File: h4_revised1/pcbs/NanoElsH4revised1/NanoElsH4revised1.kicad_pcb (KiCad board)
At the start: 4 copper layers, 141 x 86 mm, 142 parts, among them Q1 SI2302ADS-T1, Q10 SI2302ADS-T1, Q11 SI2302ADS-T1, Q12 SI2302ADS-T1, Q13 SI2302ADS-T1, Q14 SI2302ADS-T1, Q15 SI2302ADS-T1, Q16 SI2302ADS-T1, Q18 SI2302ADS-T1, Q2 SI2302ADS-T1, Q3 S9013W, Q4 S9013W, Q5 SI2302ADS-T1, Q6 SI2302ADS-T1, Q7 SI2302ADS-T1, Q8 SI2302ADS-T1, Q9 SI2302ADS-T1

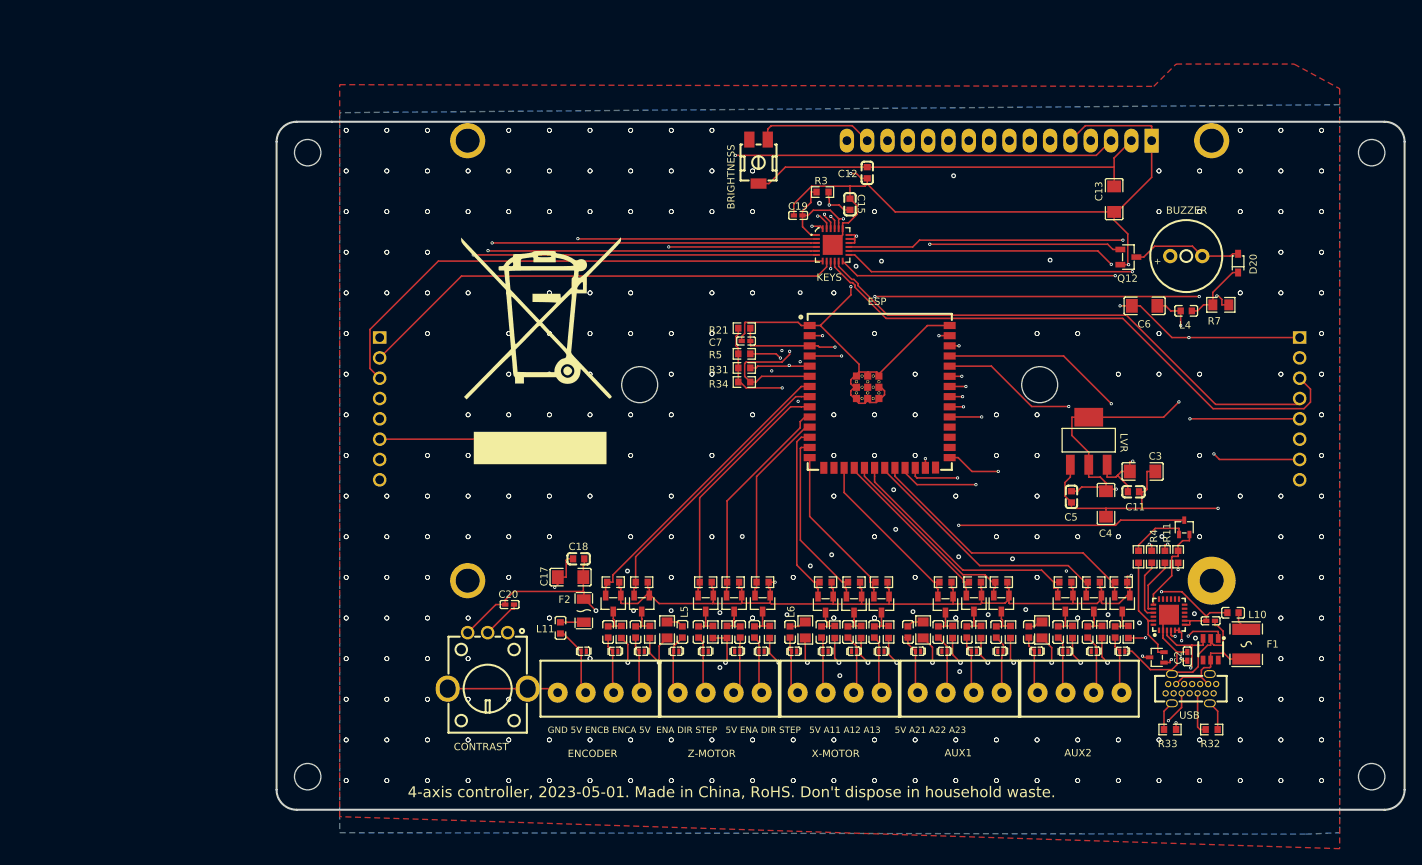
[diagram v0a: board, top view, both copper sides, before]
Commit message: - Added actual KiCad 8 files (layout ready, but some cosmetic documentation ToDo's)
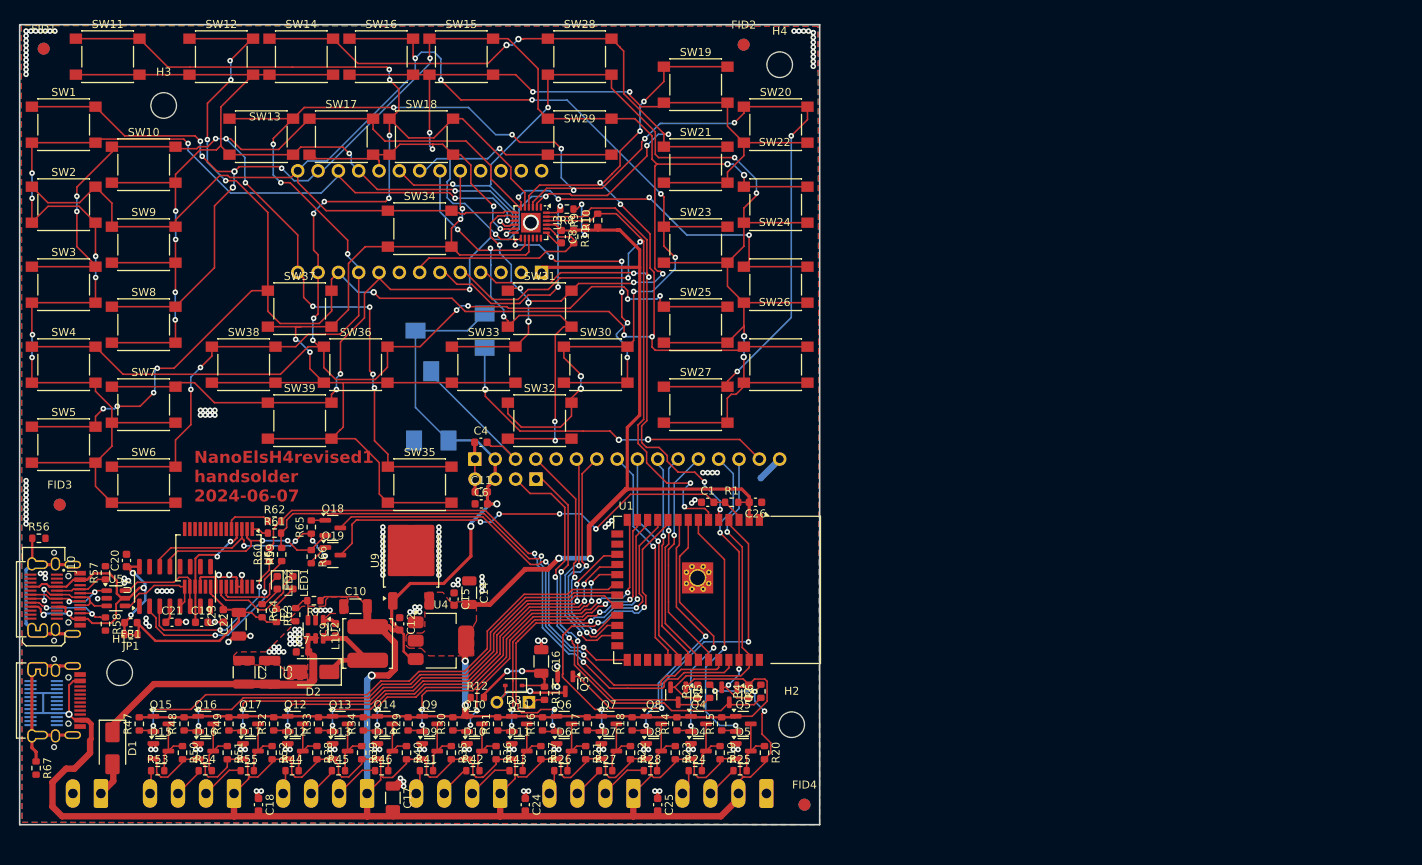
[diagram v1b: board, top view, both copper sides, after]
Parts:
- removed AUX1, AUX2, ENCODER, X-MOTOR, Z-MOTOR: DB2EVC-3.5-4P-GN, NanoElsH4:CONN-TH_4P-P3.50_DB2EVC-3.5-4P-GN
- removed BRIGHTNESS: 1k, NanoElsH4:RES-ADJ-SMD_3P-L4.5-W4.5-P2.30-LS6.2-BL-FS
- removed BUZZER: QMB-09B-03, NanoElsH4:BUZ-TH_BD9.0-P4.00-D0.6-FD
- removed C13, C3: 10uF, NanoElsH4:C1206
- removed COLS, ROWS: MF254V-11-08-0540, NanoElsH4:HDR-TH_8P-P2.54-V-F-3
- removed CONTRAST: 10kΩ, NanoElsH4:RES-TH_RK09K113004U
- removed D20: 1N4148WS T4, NanoElsH4:SOD-323_L1.8-W1.3-LS2.5-RD
- removed D21, D22, D23, D24, D25, D26, D27, D28, D29, D30, D31, D32, D33, D34, D35, D36, D37, D38, D39: KESD9B5VL, NanoElsH4:X1-DFN1006-2_L1.0-W0.6-P0.65-BI
- removed ESP: ESP32-S3-WROOM-1U-N16R2, NanoElsH4:WIRELM-SMD_ESP32-S3-WROOM-1U
- removed F1: SMD1812P030TF, NanoElsH4:F1812
- removed F2: nSMD010, NanoElsH4:F1206
- removed Hole_gge6227889318616504: Hole_gge6227889318616504, NanoElsH4:Hole_gge6227889318616504
- removed Hole_gge6227889318616534: Hole_gge6227889318616534, NanoElsH4:Hole_gge6227889318616534
- removed Hole_gge6227889318616549: Hole_gge6227889318616549, NanoElsH4:Hole_gge6227889318616549
- removed Hole_gge6227889318616564: Hole_gge6227889318616564, NanoElsH4:Hole_gge6227889318616564
- removed Hole_gge813785: Hole_gge813785, NanoElsH4:Hole_gge813785
- removed Hole_gge813800: Hole_gge813800, NanoElsH4:Hole_gge813800
- removed KEYS: TCA8418RTWR, NanoElsH4:WQFN-24_L4.0-W4.0-P0.50-TL-EP2.5
- removed L10, L11, L2, L22, L23, L24, L25, L26, L27, L28, L29, L3, L31, L32, L33, L34, L36, L4, L5, L6: 120Ω, NanoElsH4:L0603
- removed LCD: LCD2004, NanoElsH4:LCD2004-PHT
- removed LVR: AMS1117-3.3, NanoElsH4:SOT-223-3_L6.4-W3.5-P2.30-LS7.0-BR
- removed TV1: SRV05-4-P-T7, NanoElsH4:SOT-23-6_L2.9-W1.6-P0.95-LS2.8-BR
- removed USB: 918-468K2029E50000, NanoElsH4:USB-C-TH_918-468K2029E50000
- removed USB2UART: CH9102F, NanoElsH4:QFN-24_L4.0-W4.0-P0.50-BL-EP2.5
- added BZ1: Buzzer, Buzzer_Beeper:MagneticBuzzer_PUI_AT-0927-TT-6-R, B.Cu at (113.7, 134.7)
- added C10: NP, Capacitor_SMD:C_1206_3216Metric, F.Cu at (92.0, 122.7)
- added C14: 10u, Capacitor_SMD:C_1206_3216Metric, F.Cu at (106.2, 121.0)
- added C16: 10u, Capacitor_SMD:C_1206_3216Metric, F.Cu at (115.2, 129.6)
- added C21: NP, Capacitor_SMD:C_0603_1608Metric, F.Cu at (69.0, 124.7)
- added C22: 4u7, Capacitor_SMD:C_1206_3216Metric, F.Cu at (77.4, 125.0)
- added C23: 100n, Capacitor_SMD:C_0603_1608Metric, F.Cu at (75.5, 123.9)
- added C24: 100n, Capacitor_SMD:C_0603_1608Metric, F.Cu at (113.2, 147.5)
- added C25: 100n, Capacitor_SMD:C_0603_1608Metric, F.Cu at (129.8, 147.5)
- added C26: 100n, Capacitor_SMD:C_0603_1608Metric, F.Cu at (142.0, 109.7)
- added C8: 100n, Capacitor_SMD:C_0603_1608Metric, F.Cu at (117.7, 76.5)
- added C9: NP, Capacitor_SMD:C_0603_1608Metric, F.Cu at (89.5, 125.6)
- added D1: NP, Diode_SMD:D_SMA, F.Cu at (61.6, 140.4)
- added D10: BAS40-04, Package_TO_SOT_SMD:SOT-23, F.Cu at (106.8, 140.8)
- added D11: BAS40-04, Package_TO_SOT_SMD:SOT-23, F.Cu at (112.5, 140.8)
- added D12: BAS40-04, Package_TO_SOT_SMD:SOT-23, F.Cu at (84.5, 140.8)
- added D13: BAS40-04, Package_TO_SOT_SMD:SOT-23, F.Cu at (90.0, 140.8)
- added D14: BAS40-04, Package_TO_SOT_SMD:SOT-23, F.Cu at (95.7, 140.8)
- added D15: BAS40-04, Package_TO_SOT_SMD:SOT-23, F.Cu at (67.7, 140.8)
- added D16: BAS40-04, Package_TO_SOT_SMD:SOT-23, F.Cu at (73.2, 140.8)
- added D17: BAS40-04, Package_TO_SOT_SMD:SOT-23, F.Cu at (78.8, 140.8)
- added D2: NP, Diode_SMD:D_SMA, F.Cu at (86.7, 130.9)
- added D3: 1N4148W, Diode_SMD:D_SOD-323, F.Cu at (111.8, 132.6)
- added D4: BAS40-04, Package_TO_SOT_SMD:SOT-23, F.Cu at (134.8, 140.8)
- added D5: BAS40-04, Package_TO_SOT_SMD:SOT-23, F.Cu at (140.4, 140.8)
- added D6: BAS40-04, Package_TO_SOT_SMD:SOT-23, F.Cu at (118.0, 140.8)
- added D7: BAS40-04, Package_TO_SOT_SMD:SOT-23, F.Cu at (123.7, 140.8)
- added D8: BAS40-04, Package_TO_SOT_SMD:SOT-23, F.Cu at (129.2, 140.8)
- added D9: BAS40-04, Package_TO_SOT_SMD:SOT-23, F.Cu at (101.2, 140.8)
- added FB1: NP, Inductor_SMD:L_0603_1608Metric, F.Cu at (63.9, 124.8)
- added FID1: ~, Fiducial:Fiducial_1.5mm_Mask3mm, F.Cu at (53.0, 53.0)
- added FID2: ~, Fiducial:Fiducial_1.5mm_Mask3mm, F.Cu at (140.5, 52.5)
- added FID3: ~, Fiducial:Fiducial_1.5mm_Mask3mm, F.Cu at (55.0, 110.0)
- added FID4: ~, Fiducial:Fiducial_1.5mm_Mask3mm, F.Cu at (148.1, 147.5)
- added FID5: ~, Fiducial:Fiducial_1.5mm_Mask3mm, B.Cu at (53.0, 53.0)
- added FID6: ~, Fiducial:Fiducial_1.5mm_Mask3mm, B.Cu at (140.5, 52.5)
- added FID7: ~, Fiducial:Fiducial_1.5mm_Mask3mm, B.Cu at (55.0, 110.0)
- added FID8: ~, Fiducial:Fiducial_1.5mm_Mask3mm, B.Cu at (148.1, 147.5)
- added H1: ~, MountingHole:MountingHole_3.2mm_M3, F.Cu at (62.5, 131.0)
- added H2: ~, MountingHole:MountingHole_3.2mm_M3, F.Cu at (146.5, 137.5)
- added H3: ~, MountingHole:MountingHole_3.2mm_M3, F.Cu at (68.0, 60.1)
- added H4: ~, MountingHole:MountingHole_3.2mm_M3, F.Cu at (145.0, 55.0)
- added J1: NP, Connector_Phoenix_MC:PhoenixContact_MCV_1,5_2-G-3.5_1x02_P3.50mm_Vertical, B.Cu at (60.1, 146.1)
- added J10: USB_C_Receptacle_USB2.0_16P, els_kicad_lib:USB_C_HorVert_top_GCT-JAE-HRO_USB4160-DX07S024WJ3R400-C31M12, F.Cu at (53.0, 121.5)
- added J2: LCD-I2C, Connector_PinHeader_2.54mm:PinHeader_1x04_P2.54mm_Horizontal, B.Cu at (114.5, 106.8)
- added J3: Screw_Terminal_01x04, Connector_Phoenix_MC:PhoenixContact_MCV_1,5_4-G-3.5_1x04_P3.50mm_Vertical, B.Cu at (143.3, 146.1)
- added J4: Screw_Terminal_01x04, Connector_Phoenix_MC:PhoenixContact_MCV_1,5_4-G-3.5_1x04_P3.50mm_Vertical, B.Cu at (126.7, 146.1)
- added J5: Screw_Terminal_01x04, Connector_Phoenix_MC:PhoenixContact_MCV_1,5_4-G-3.5_1x04_P3.50mm_Vertical, B.Cu at (110.1, 146.1)
- added J6: Screw_Terminal_01x04, Connector_Phoenix_MC:PhoenixContact_MCV_1,5_4-G-3.5_1x04_P3.50mm_Vertical, B.Cu at (93.4, 146.1)
- added J7: Screw_Terminal_01x04, Connector_Phoenix_MC:PhoenixContact_MCV_1,5_4-G-3.5_1x04_P3.50mm_Vertical, B.Cu at (76.8, 146.1)
- added J9: USB_C_Receptacle_USB2.0_16P, els_kicad_lib:USB_C_HorVert_topbot_GCT-JAE-HRO_USB4160-DX07S024WJ3R400-C31M12, B.Cu at (53.0, 134.8)
- added JP1: ~, els_kicad_lib:R_0603_1608Metric_shorted, F.Cu at (63.9, 126.2)
- added LCD1: NP, els_kicad_lib:LCD_HD44780_header_horizontal, B.Cu at (106.9, 104.3)
- added LED1: NP, LED_SMD:LED_0603_1608Metric, F.Cu at (84.2, 119.8)
- added LED2: NP, LED_SMD:LED_0603_1608Metric, F.Cu at (82.2, 119.8)
- added Q17: 2N7002, Package_TO_SOT_SMD:SOT-23, F.Cu at (78.8, 137.4)
- added Q19: BC846B, Package_TO_SOT_SMD:SOT-23, F.Cu at (89.2, 116.3)
- added R10: 4k7, Resistor_SMD:R_0603_1608Metric, F.Cu at (122.2, 74.5)
- added R46: 120R, Resistor_SMD:R_0603_1608Metric, F.Cu at (95.2, 143.2)
- added R47: 4k7, Resistor_SMD:R_0603_1608Metric, F.Cu at (65.0, 137.4)
- added R50: 4k7, Resistor_SMD:R_0603_1608Metric, F.Cu at (70.3, 141.0)
- added R51: 4k7, Resistor_SMD:R_0603_1608Metric, F.Cu at (76.0, 141.0)
- added R52: 4k7, Resistor_SMD:R_0603_1608Metric, F.Cu at (81.5, 141.0)
- added R53: 120R, Resistor_SMD:R_0603_1608Metric, F.Cu at (67.2, 143.2)
- added R54: 120R, Resistor_SMD:R_0603_1608Metric, F.Cu at (73.2, 143.2)
- added R55: 120R, Resistor_SMD:R_0603_1608Metric, F.Cu at (78.5, 143.2)
- added R56: 1M, Resistor_SMD:R_0603_1608Metric, F.Cu at (52.4, 114.2)
- added R57: 5k1, Resistor_SMD:R_0603_1608Metric, F.Cu at (60.7, 118.5)
- added R58: 5k1, Resistor_SMD:R_0603_1608Metric, F.Cu at (60.7, 124.9)
- added R59: NP, Resistor_SMD:R_0603_1608Metric, F.Cu at (82.8, 116.2)
- added R60: NP, Resistor_SMD:R_0603_1608Metric, F.Cu at (81.2, 116.2)
- added R61: 470R, Resistor_SMD:R_0603_1608Metric, F.Cu at (81.8, 113.5)
- added R62: 470R, Resistor_SMD:R_0603_1608Metric, F.Cu at (81.8, 112.0)
- added R63: NP, Resistor_SMD:R_0603_1608Metric, F.Cu at (82.1, 123.8)
- added R64: NP, Resistor_SMD:R_0603_1608Metric, F.Cu at (80.3, 123.2)
- added R65: 10k, Resistor_SMD:R_0603_1608Metric, F.Cu at (86.5, 112.8)
- added R66: 10k, Resistor_SMD:R_0603_1608Metric, F.Cu at (86.5, 116.5)
- added R67: 1M, Resistor_SMD:R_0603_1608Metric, F.Cu at (52.0, 142.9)
- added R8: 4k7, Resistor_SMD:R_0603_1608Metric, F.Cu at (118.4, 73.0)
- added R9: 4k7, Resistor_SMD:R_0603_1608Metric, F.Cu at (120.8, 74.5)
- added RV1: NP, Potentiometer_SMD:Potentiometer_ACP_CA6-VSMD_Vertical, B.Cu at (103.8, 88.2)
- added RV2: NP, Potentiometer_SMD:Potentiometer_ACP_CA6-VSMD_Vertical, B.Cu at (101.5, 97.7)
- added SW1: 6X6SMD, Button_Switch_SMD:SW_Push_1P1T_NO_6x6mm_H9.5mm, F.Cu at (55.5, 62.5)
- added SW10: 6X6SMD, Button_Switch_SMD:SW_Push_1P1T_NO_6x6mm_H9.5mm, F.Cu at (65.5, 67.5)
- added SW11: 6X6SMD, Button_Switch_SMD:SW_Push_1P1T_NO_6x6mm_H9.5mm, F.Cu at (61.0, 54.0)
- added SW12: 6X6SMD, Button_Switch_SMD:SW_Push_1P1T_NO_6x6mm_H9.5mm, F.Cu at (75.2, 54.0)
- added SW13: 6X6SMD, Button_Switch_SMD:SW_Push_1P1T_NO_6x6mm_H9.5mm, F.Cu at (80.2, 64.0)
- added SW14: 6X6SMD, Button_Switch_SMD:SW_Push_1P1T_NO_6x6mm_H9.5mm, F.Cu at (85.2, 54.0)
- added SW15: 6X6SMD, Button_Switch_SMD:SW_Push_1P1T_NO_6x6mm_H9.5mm, F.Cu at (105.2, 54.0)
- added SW16: 6X6SMD, Button_Switch_SMD:SW_Push_1P1T_NO_6x6mm_H9.5mm, F.Cu at (95.2, 54.0)
- added SW17: 6X6SMD, Button_Switch_SMD:SW_Push_1P1T_NO_6x6mm_H9.5mm, F.Cu at (90.2, 64.0)
- added SW18: 6X6SMD, Button_Switch_SMD:SW_Push_1P1T_NO_6x6mm_H9.5mm, F.Cu at (100.2, 64.0)
- added SW19: 6X6SMD, Button_Switch_SMD:SW_Push_1P1T_NO_6x6mm_H9.5mm, F.Cu at (134.5, 57.5)
- added SW2: 6X6SMD, Button_Switch_SMD:SW_Push_1P1T_NO_6x6mm_H9.5mm, F.Cu at (55.5, 72.5)
- added SW20: 6X6SMD, Button_Switch_SMD:SW_Push_1P1T_NO_6x6mm_H9.5mm, F.Cu at (144.5, 62.5)
- added SW21: 6X6SMD, Button_Switch_SMD:SW_Push_1P1T_NO_6x6mm_H9.5mm, F.Cu at (134.5, 67.5)
- added SW22: 6X6SMD, Button_Switch_SMD:SW_Push_1P1T_NO_6x6mm_H9.5mm, F.Cu at (144.5, 72.5)
- added SW23: 6X6SMD, Button_Switch_SMD:SW_Push_1P1T_NO_6x6mm_H9.5mm, F.Cu at (134.5, 77.5)
- added SW24: 6X6SMD, Button_Switch_SMD:SW_Push_1P1T_NO_6x6mm_H9.5mm, F.Cu at (144.5, 82.5)
- added SW25: 6X6SMD, Button_Switch_SMD:SW_Push_1P1T_NO_6x6mm_H9.5mm, F.Cu at (134.5, 87.5)
- added SW26: 6X6SMD, Button_Switch_SMD:SW_Push_1P1T_NO_6x6mm_H9.5mm, F.Cu at (144.5, 92.5)
- added SW27: 6X6SMD, Button_Switch_SMD:SW_Push_1P1T_NO_6x6mm_H9.5mm, F.Cu at (134.5, 97.5)
- added SW28: 6X6SMD, Button_Switch_SMD:SW_Push_1P1T_NO_6x6mm_H9.5mm, F.Cu at (120.0, 54.0)
- added SW29: 6X6SMD, Button_Switch_SMD:SW_Push_1P1T_NO_6x6mm_H9.5mm, F.Cu at (120.0, 64.0)
- added SW3: 6X6SMD, Button_Switch_SMD:SW_Push_1P1T_NO_6x6mm_H9.5mm, F.Cu at (55.5, 82.5)
- added SW30: 6X6SMD, Button_Switch_SMD:SW_Push_1P1T_NO_6x6mm_H9.5mm, F.Cu at (122.0, 92.5)
- added SW31: 6X6SMD, Button_Switch_SMD:SW_Push_1P1T_NO_6x6mm_H9.5mm, F.Cu at (115.0, 85.5)
- added SW32: 6X6SMD, Button_Switch_SMD:SW_Push_1P1T_NO_6x6mm_H9.5mm, F.Cu at (115.0, 99.5)
- added SW33: 6X6SMD, Button_Switch_SMD:SW_Push_1P1T_NO_6x6mm_H9.5mm, F.Cu at (108.0, 92.5)
- added SW34: 6X6SMD, Button_Switch_SMD:SW_Push_1P1T_NO_6x6mm_H9.5mm, F.Cu at (100.0, 75.5)
- added SW35: 6X6SMD, Button_Switch_SMD:SW_Push_1P1T_NO_6x6mm_H9.5mm, F.Cu at (100.0, 107.5)
- added SW36: 6X6SMD, Button_Switch_SMD:SW_Push_1P1T_NO_6x6mm_H9.5mm, F.Cu at (92.0, 92.5)
- added SW37: 6X6SMD, Button_Switch_SMD:SW_Push_1P1T_NO_6x6mm_H9.5mm, F.Cu at (85.0, 85.5)
- added SW38: 6X6SMD, Button_Switch_SMD:SW_Push_1P1T_NO_6x6mm_H9.5mm, F.Cu at (78.0, 92.5)
- added SW39: 6X6SMD, Button_Switch_SMD:SW_Push_1P1T_NO_6x6mm_H9.5mm, F.Cu at (85.0, 99.5)
- added SW4: 6X6SMD, Button_Switch_SMD:SW_Push_1P1T_NO_6x6mm_H9.5mm, F.Cu at (55.5, 92.5)
- added SW5: 6X6SMD, Button_Switch_SMD:SW_Push_1P1T_NO_6x6mm_H9.5mm, F.Cu at (55.5, 102.5)
- added SW6: 6X6SMD, Button_Switch_SMD:SW_Push_1P1T_NO_6x6mm_H9.5mm, F.Cu at (65.5, 107.5)
- added SW7: 6X6SMD, Button_Switch_SMD:SW_Push_1P1T_NO_6x6mm_H9.5mm, F.Cu at (65.5, 97.5)
- added SW8: 6X6SMD, Button_Switch_SMD:SW_Push_1P1T_NO_6x6mm_H9.5mm, F.Cu at (65.5, 87.5)
- added SW9: 6X6SMD, Button_Switch_SMD:SW_Push_1P1T_NO_6x6mm_H9.5mm, F.Cu at (65.5, 77.5)
- added U1: ESP32-S3-WROOM-1, els_kicad_lib:ESP32-S3-WROOM-1_bighole, F.Cu at (137.2, 120.7)
- added U2: NP, Package_TO_SOT_SMD:SOT-23-6, F.Cu at (87.0, 125.6)
- added U3: TCA8418RTW, Package_DFN_QFN:WQFN-24-1EP_4x4mm_P0.5mm_EP2.45x2.45mm, F.Cu at (113.9, 74.8)
- added U4: NP, Package_TO_SOT_SMD:SOT-223-3_TabPin2, F.Cu at (102.7, 127.0)
- added U5: USBLC6-2SC6, Package_TO_SOT_SMD:SOT-23-6, F.Cu at (62.0, 121.7)
- added U6: FT232RL, Package_SO:SSOP-28_5.3x10.2mm_P0.65mm, F.Cu at (74.8, 116.7)
- added U7: NP, Package_SO:SOIC-16_3.9x9.9mm_P1.27mm, F.Cu at (69.4, 120.2)
- added U8: NP, els_kicad_lib:Adafruit_STEMMA_TCA8418, B.Cu at (100.0, 74.6)
- added U9: LF33ABDT, Package_TO_SOT_SMD:TO-252-2, F.Cu at (98.9, 117.0)
- C1: value 1uF -> 1u; footprint NanoElsH4:C0402 -> Capacitor_SMD:C_0603_1608Metric
- C11, C12, C15, C18: value 100nF -> 100n; footprint NanoElsH4:C0603 -> Capacitor_SMD:C_0603_1608Metric
- C17: value 10uF -> 2u2; footprint NanoElsH4:C1206 -> Capacitor_SMD:C_1206_3216Metric
- C19: value 1nF -> 100n; footprint NanoElsH4:C0402 -> Capacitor_SMD:C_0603_1608Metric
- C2: value 1uF -> NP; footprint NanoElsH4:C0402 -> Capacitor_SMD:C_1210_3225Metric
- C20: value 1nF -> NP; footprint NanoElsH4:C0402 -> Capacitor_SMD:C_0603_1608Metric
- C4: value 10uF -> NP; footprint NanoElsH4:C1206 -> Capacitor_SMD:C_0603_1608Metric
- C5: value 100nF -> NP; footprint NanoElsH4:C0603 -> Capacitor_SMD:C_1210_3225Metric
- C6: value 10uF -> 1u; footprint NanoElsH4:C1206 -> Capacitor_SMD:C_0603_1608Metric
- C7: value 1uF -> NP; footprint NanoElsH4:C0402 -> Capacitor_SMD:C_0603_1608Metric
- L1: value 120Ω -> NP; footprint NanoElsH4:L0603 -> Inductor_SMD:L_TDK_VLS6045EX_VLS6045AF
- Q1, Q10, Q11, Q12, Q13, Q14, Q15, Q16, Q2, Q5, Q6, Q7, Q8, Q9: value SI2302ADS-T1 -> 2N7002; footprint NanoElsH4:SOT-23-3_L2.9-W1.3-P1.90-LS2.4-BR -> Package_TO_SOT_SMD:SOT-23
- Q18: value SI2302ADS-T1 -> BC846B; footprint NanoElsH4:SOT-23-3_L2.9-W1.3-P1.90-LS2.4-BR -> Package_TO_SOT_SMD:SOT-23
- Q3, Q4: value S9013W -> 2N7002; footprint NanoElsH4:SOT-323-3_L2.0-W1.3-P1.30-LS2.1-BR -> Package_TO_SOT_SMD:SOT-23
- R1, R15, R17, R18, R19, R20, R22, R23, R29, R30, R35, R38, R39, R40, R48, R49, R6: value 2kΩ -> 4k7; footprint NanoElsH4:R0603 -> Resistor_SMD:R_0603_1608Metric
- R11, R4: value 470Ω -> 4k7; footprint NanoElsH4:R0603 -> Resistor_SMD:R_0603_1608Metric
- R12: value 200Ω -> 120R; footprint NanoElsH4:R0805 -> Resistor_SMD:R_0603_1608Metric
- R13: value 10kΩ -> 10R; footprint NanoElsH4:R0603 -> Resistor_SMD:R_0603_1608Metric
- R14: value 10kΩ -> 4k7; footprint NanoElsH4:R0603 -> Resistor_SMD:R_0603_1608Metric
- R16, R36, R37: value 200Ω -> 4k7; footprint NanoElsH4:R0805 -> Resistor_SMD:R_0603_1608Metric
- R2: value 2kΩ -> NP; footprint NanoElsH4:R0603 -> Resistor_SMD:R_0603_1608Metric
- R21, R3, R31, R32, R33, R34, R5: value 5.1kΩ -> 4k7; footprint NanoElsH4:R0603 -> Resistor_SMD:R_0603_1608Metric
- R24, R25, R26, R27, R28, R41, R42, R43, R44, R45: value 2kΩ -> 120R; footprint NanoElsH4:R0603 -> Resistor_SMD:R_0603_1608Metric
- R7: value 100Ω -> NP; footprint NanoElsH4:R0805 -> Resistor_SMD:R_0603_1608Metric
- moved Q12 119.4 mm to (84.5, 137.4), turned to 0 degrees
- moved R7 119.2 mm to (86.8, 122.0), turned to 180 degrees
- moved C2 117.9 mm to (78.0, 130.9), turned to -90 degrees
- moved Q15 117.6 mm to (67.7, 137.4), turned to 0 degrees
- moved R32 117.3 mm to (81.8, 137.4), turned to 90 degrees
- moved Q16 115.6 mm to (73.2, 137.4), turned to 0 degrees
- moved R48 111.6 mm to (70.5, 137.4), turned to 90 degrees
- moved R33 106.4 mm to (87.3, 137.4), turned to 90 degrees
- moved R44 106.3 mm to (84.0, 143.2)
- moved R49 106.1 mm to (76.2, 137.4)
- moved C5 102.6 mm to (81.2, 130.9)
- moved R45 100.2 mm to (89.8, 143.2), turned to 0 degrees
- moved Q18 92.1 mm to (89.1, 112.9), turned to 0 degrees
- moved C19 90.3 mm to (72.8, 124.7)
- moved R38 88.0 mm to (87.2, 141.0), turned to -90 degrees
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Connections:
- C1 pad 2: 5V -> /ESP_EN
- C11 pad 2: 5V -> +5V
- C12 pad 2: 5V -> +5V
- C15 pad 1: 3V -> GND
- C15 pad 2: GND -> +3V3
- C17 pad 2: 5V -> +5V
- C18 pad 2: 5V -> +5V
- C19 pad 1: GND -> Net-(U6-3V3OUT)
- C19 pad 2: KEYS_1 -> GND
- C2 pad 1: USB2UART_5 -> GND
- C2 pad 2: GND -> VDC
- C20 pad 1: 5V -> /USB_to_ESP/VBUS_USB
- C20 pad 2: LCD_3 -> GND
- C4 pad 2: 3V -> /LCD_CONTRAST
- C5 pad 1: 3V -> GND
- C5 pad 2: GND -> VDC
- C6 pad 2: 3V -> +5V
- C7 pad 1: EN -> GND
- C7 pad 2: GND -> VDC
- L1 pad 1: ZSTEP-5V -> Net-(D2-K)
- L1 pad 2: L1_2 -> +5V
- Q1 pad 1: 3V -> +3V3
- Q1 pad 2: ZSTEP-3V -> /LCD_D7-I2SCL
- Q1 pad 3: L1_2 -> Net-(J2-Pin_1)
- Q10 pad 1: 3V -> +3V3
- Q10 pad 2: ENCB-3V -> /XDIR_3V
- Q10 pad 3: Q10_3 -> Net-(Q10-D)
- Q11 pad 1: 3V -> +3V3
- Q11 pad 2: ENCA-3V -> /XENA_3V
- Q11 pad 3: Q11_3 -> Net-(Q11-D)
- Q12 pad 1: BUZZ -> +3V3
- Q12 pad 2: GND -> /AUX11_3V
- Q12 pad 3: BUZZER_2 -> Net-(Q12-D)
- Q13 pad 1: 3V -> +3V3
- Q13 pad 2: AUX13-3V -> /AUX12_3V
- Q13 pad 3: L31_2 -> Net-(Q13-D)
- Q14 pad 1: 3V -> +3V3
- Q14 pad 2: AUX12-3V -> /AUX13_3V
- Q14 pad 3: L32_2 -> Net-(Q14-D)
- Q15 pad 1: 3V -> +3V3
- Q15 pad 2: AUX22-3V -> /AUX21_3V
- Q15 pad 3: Q15_3 -> Net-(Q15-D)
- Q16 pad 1: 3V -> +3V3
- Q16 pad 2: AUX23-3V -> /AUX22_3V
- Q16 pad 3: Q16_3 -> Net-(Q16-D)
- Q18 pad 1: 3V -> Net-(Q18-B)
- Q18 pad 2: AUX21-3V -> /USB_to_ESP/~{DTR}
- Q18 pad 3: Q18_3 -> /ESP_BOOT
- Q2 pad 1: 3V -> +3V3
- Q2 pad 2: ZDIR-3V -> /LCD_D6-I2SDA
- Q2 pad 3: L22_2 -> Net-(J2-Pin_2)
- Q3 pad 1: Q3_1 -> /ESP_BUZZER
- Q3 pad 2: USB2UART_23 -> GND
- Q3 pad 3: BOOT -> Net-(BZ1--)
- Q4 pad 1: Q4_1 -> +3V3
- Q4 pad 2: USB2UART_19 -> /ENCA_3V
- Q4 pad 3: EN -> Net-(Q4-D)
- Q5 pad 1: 3V -> +3V3
- Q5 pad 2: ZENA-3V -> /ENCB_3V
- Q5 pad 3: L23_2 -> Net-(Q5-D)
- Q6 pad 1: 3V -> +3V3
- Q6 pad 2: XENA-3V -> /ZSTEP_3V
- Q6 pad 3: Q6_3 -> Net-(Q6-D)
- Q7 pad 1: 3V -> +3V3
- Q7 pad 2: XDIR-3V -> /ZDIR_3V
- Q7 pad 3: Q7_3 -> Net-(Q7-D)
- Q8 pad 1: 3V -> +3V3
- Q8 pad 2: XSTEP-3V -> /ZENA_3V
- Q8 pad 3: Q8_3 -> Net-(Q8-D)
- Q9 pad 1: 3V -> +3V3
- Q9 pad 2: AUX11-3V -> /XSTEP_3V
- Q9 pad 3: L27_2 -> Net-(Q9-D)
- R1 pad 1: ZSTEP-3V -> /ESP_EN
- R1 pad 2: 3V -> +3V3
- R11 pad 1: USB2UART_20 -> +3V3
- R11 pad 2: TX -> /KEY_~{RST}
- R12 pad 1: 5V -> +3V3
- R12 pad 2: L6_1 -> Net-(D3-K)
- R13 pad 1: USB2UART_19 -> Net-(D3-K)
- R13 pad 2: Q3_1 -> Net-(BZ1-+)
- R14 pad 1: USB2UART_23 -> /ENCA_3V
- R14 pad 2: Q4_1 -> +3V3
- R15 pad 1: ZDIR-3V -> /ENCB_3V
- R15 pad 2: 3V -> +3V3
- R16 pad 1: 5V -> /ZSTEP_3V
- R16 pad 2: L5_1 -> +3V3
- R17 pad 1: 5V -> /ZDIR_3V
- R17 pad 2: L23_2 -> +3V3
- R18 pad 1: ZENA-3V -> /ZENA_3V
- R18 pad 2: 3V -> +3V3
- R19 pad 1: XENA-3V -> Net-(Q4-D)
- R19 pad 2: 3V -> +5V
- R2 pad 1: 5V -> GND
- R2 pad 2: L1_2 -> Net-(U2-FB)
- R20 pad 1: 5V -> Net-(Q5-D)
- R20 pad 2: Q6_3 -> +5V
- R21 pad 1: 3V -> Net-(Q6-D)
- R21 pad 2: EN -> +5V
- R22 pad 1: XDIR-3V -> Net-(Q7-D)
- R22 pad 2: 3V -> +5V
- R23 pad 1: 5V -> Net-(Q8-D)
- R23 pad 2: Q7_3 -> +5V
- R24 pad 1: XSTEP-3V -> /NanoElsH4revised1_IO/ENCA_5V
- R24 pad 2: 3V -> Net-(Q4-D)
- R25 pad 1: 5V -> /NanoElsH4revised1_IO/ENCB_5V
- R25 pad 2: Q8_3 -> Net-(Q5-D)
- R26 pad 1: 5V -> Net-(J4-Pin_4)
- R26 pad 2: L27_2 -> Net-(Q6-D)
- R27 pad 1: AUX11-3V -> Net-(J4-Pin_3)
- R27 pad 2: 3V -> Net-(Q7-D)
- R28 pad 1: ENCB-3V -> Net-(J4-Pin_2)
- R28 pad 2: 3V -> Net-(Q8-D)
- R29 pad 1: 5V -> /XSTEP_3V
- R29 pad 2: Q10_3 -> +3V3
- R3 pad 1: 3V -> /LCD_D7-I2SCL
- R3 pad 2: KEYS_1 -> +3V3
- R30 pad 1: ENCA-3V -> /XDIR_3V
- R30 pad 2: 3V -> +3V3
- R31 pad 1: 3V -> /XENA_3V
- R31 pad 2: SCL -> +3V3
- R32 pad 1: USB_B5 -> /AUX11_3V
- R32 pad 2: GND -> +3V3
- R33 pad 1: GND -> /AUX12_3V
- R33 pad 2: USB_A5 -> +3V3
- R34 pad 1: 3V -> /AUX13_3V
- R34 pad 2: SDA -> +3V3
- R35 pad 1: 5V -> Net-(Q9-D)
- R35 pad 2: Q11_3 -> +5V
- R36 pad 1: 5V -> Net-(Q10-D)
- R36 pad 2: L2_1 -> +5V
- R37 pad 1: 5V -> Net-(Q11-D)
- R37 pad 2: L3_1 -> +5V
- R38 pad 1: 5V -> Net-(Q12-D)
- R38 pad 2: L31_2 -> +5V
- R39 pad 1: AUX13-3V -> Net-(Q13-D)
- R39 pad 2: 3V -> +5V
- R4 pad 1: USB2UART_21 -> /LCD_D6-I2SDA
- R4 pad 2: RX -> +3V3
- R40 pad 1: 5V -> Net-(Q14-D)
- R40 pad 2: L32_2 -> +5V
- R41 pad 1: AUX12-3V -> Net-(J5-Pin_4)
- R41 pad 2: 3V -> Net-(Q9-D)
- R42 pad 1: AUX22-3V -> Net-(J5-Pin_3)
- R42 pad 2: 3V -> Net-(Q10-D)
- R43 pad 1: 5V -> Net-(J5-Pin_2)
- R43 pad 2: Q15_3 -> Net-(Q11-D)
- R44 pad 1: AUX23-3V -> Net-(J6-Pin_4)
- R44 pad 2: 3V -> Net-(Q12-D)
- R45 pad 1: 5V -> Net-(J6-Pin_3)
- R45 pad 2: Q16_3 -> Net-(Q13-D)
- R48 pad 1: AUX21-3V -> /AUX22_3V
- R48 pad 2: 3V -> +3V3
- R49 pad 1: 5V -> /AUX23_3V
- R49 pad 2: Q18_3 -> +3V3
- R5 pad 1: 3V -> Net-(J2-Pin_1)
- R5 pad 2: INT -> +5V
- R6 pad 1: 5V -> Net-(J2-Pin_2)
- R6 pad 2: L22_2 -> +5V
- R7 pad 1: R7_1 -> +5V
- R7 pad 2: BUZZER_1 -> Net-(U2-FB)
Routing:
- net +5V: track 0.00 -> 390.1 mm, vias 0 -> 7
- net GND: track 408.4 -> 72.6 mm, vias 515 -> 173
- net 5V: track 306.0 -> 0.00 mm, vias 19 -> 0
- net 3V: track 234.6 -> 0.00 mm, vias 9 -> 0
- net /KEY_ROW4: track 0.00 -> 225.1 mm, vias 0 -> 15
- net +3V3: track 0.00 -> 220.1 mm, vias 0 -> 6
- net /KEY_ROW0: track 0.00 -> 217.3 mm, vias 0 -> 14
- net /KEY_ROW3: track 0.00 -> 213.8 mm, vias 0 -> 12
- net /KEY_ROW5: track 0.00 -> 213.6 mm, vias 0 -> 13
- net /KEY_ROW1: track 0.00 -> 205.0 mm, vias 0 -> 8
- net /KEY_ROW2: track 0.00 -> 192.6 mm, vias 0 -> 13
- net /KEY_ROW6: track 0.00 -> 170.0 mm, vias 0 -> 8
- net /KEY_COL0: track 0.00 -> 164.8 mm, vias 0 -> 9
- net /KEY_COL3: track 0.00 -> 156.9 mm, vias 0 -> 7
- net /KEY_COL1: track 0.00 -> 141.5 mm, vias 0 -> 7
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- added copper zone on F.Cu, net +3V3
- removed copper zone on In1.Cu, net GND
- removed copper zone on In2.Cu, net GND
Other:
- board size 141 x 86 mm -> 100 x 100 mm
- copper layers 4 -> 2
- board text added: "NanoElsH4revised1 handsolder 2024-06-07"
- board text removed: "4-axis controller, 2023-05-01. Made in China, RoHS. Don't dispose in household waste."
- board text removed: "C6 C5 C4 C3 C2 C1 C0 GND"
- board text removed: "GND 5V ENCB ENCA 5V ENA DIR STEP 5V ENA DIR STEP 5V A11 A12 A13 5V A21 A22 A23"
- board text removed: "R6 R5 R4 R3 R2 R1 R0 GND"
